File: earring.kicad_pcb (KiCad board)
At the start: 2 copper layers, 41.4 x 41.9 mm, 106 parts, among them J2 USB_C_Receptacle_USB2.0, Q1 Q_NMOS_SGD, Q5 light_sensor, U1 Magnetic Switch, U10 USBLC6-2P6, U20 LGS4056H, U3 RP2040, U4 W25Q16JVUXIQ, U43 TPS22913BYZVR, U44 TPS22913BYZVR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

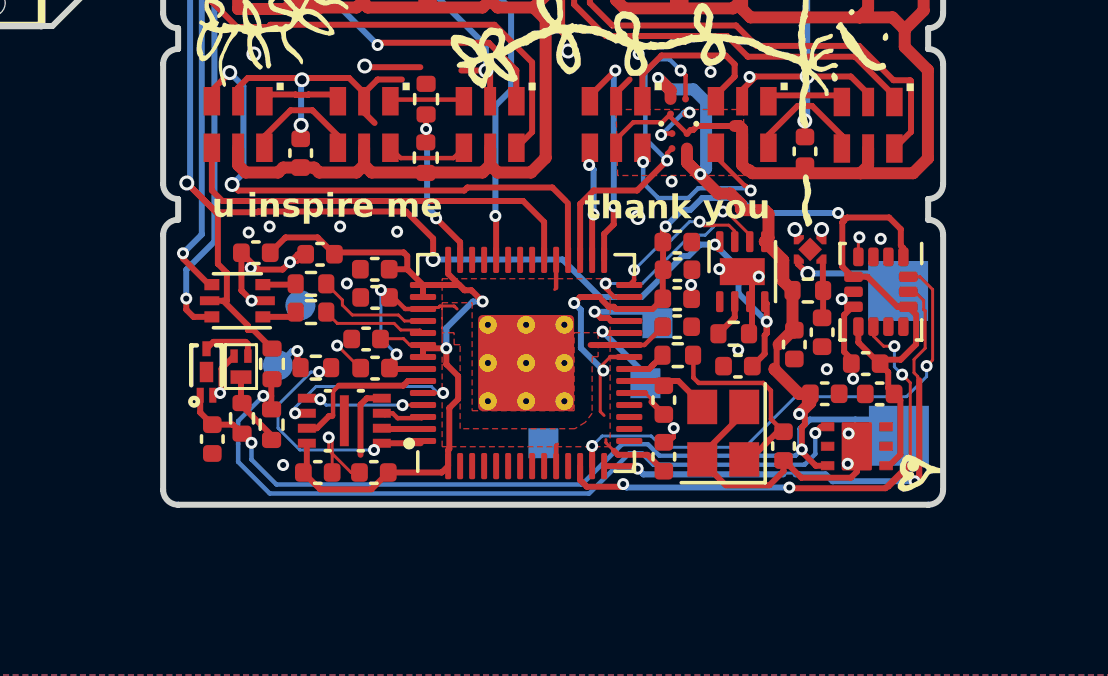
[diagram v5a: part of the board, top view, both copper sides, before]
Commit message: Had to cancel order, fixing DRC issues in progress.
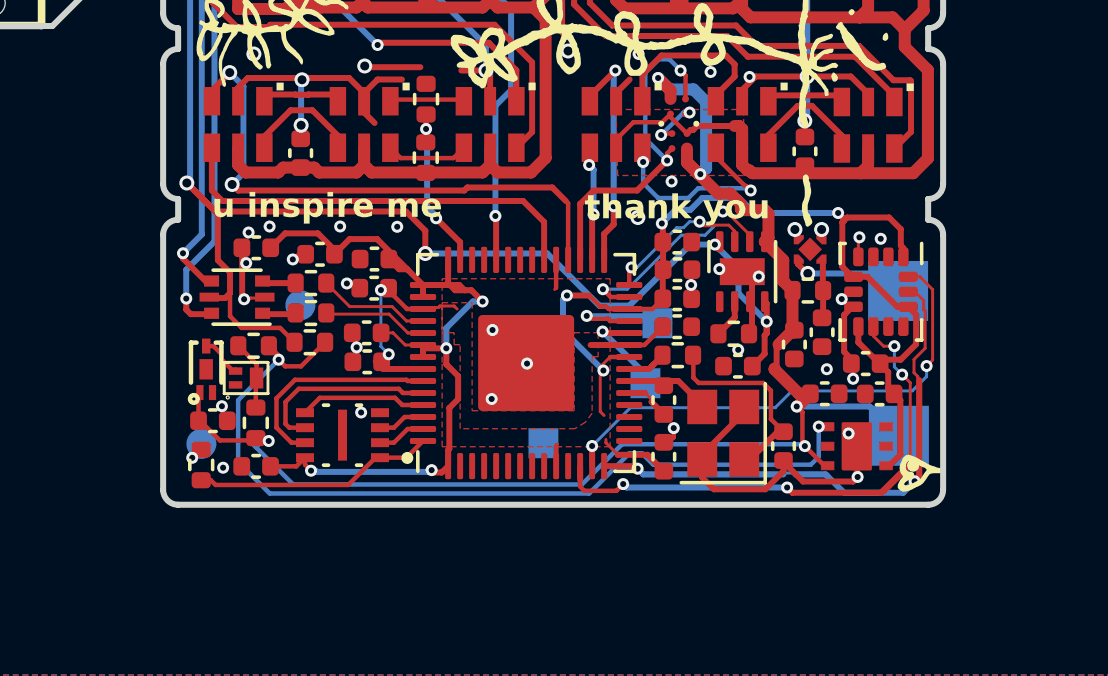
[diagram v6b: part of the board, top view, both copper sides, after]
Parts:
- removed C13: 100n, Capacitor_SMD:C_0402_1005Metric
- C1: value 100n -> 1u
- moved R1 5.01 mm to (151.3, 103.6), turned to 90 degrees
- moved TP7 3.66 mm to (151.3, 102.9)
- moved R15 2.70 mm to (153.0, 99.6), turned to 0 degrees
- moved C1 2.07 mm to (153.1, 103.6), turned to 180 degrees
- moved R2 1.45 mm to (154.9, 99.5), turned to 0 degrees
- moved C19 0.61 mm to (151.7, 102.1), turned to 0 degrees
- moved R13 0.48 mm to (153.1, 102.2)
- moved U4 0.48 mm to (156.0, 102.6)
- moved Q1 0.42 mm to (152.8, 100.7), turned to 0 degrees
- moved C18 0.34 mm to (157.0, 96.7)
- moved C8 0.33 mm to (156.8, 100.2)
- moved C10 0.31 mm to (157.0, 97.7)
- moved C11 0.21 mm to (156.8, 99.2)
- moved C12 0.17 mm to (153.1, 96.4)
- moved U10 0.12 mm to (152.5, 98.0)
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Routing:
- net GND: track 242.7 -> 230.6 mm, vias 95 -> 98
- net /3v3EN: track 25.6 -> 28.5 mm
- net /QSPI_SD3: track 5.00 -> 7.29 mm
- net +3V3: track 64.4 -> 66.4 mm, vias 6 -> 8
- net VBUS: track 55.9 -> 57.4 mm
- net /~{USB_BOOT}: track 1.87 -> 1.01 mm
- net INT: track 21.6 -> 22.2 mm
- net +1V1: track 9.60 -> 10.1 mm
- net /QSPI_SD0: track 3.97 -> 4.24 mm, vias 2 -> 0
- net /QSPI_SS: track 7.86 -> 8.06 mm, vias 2 -> 0
- net /QSPI_SCLK: track 6.18 -> 6.25 mm, vias 2 -> 0

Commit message: more clean up. looking pretty good
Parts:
- moved R12 6.82 mm to (154.6, 86.0)
- moved U43 0.27 mm to (167.3, 93.1)
- moved U8 0.20 mm to (171.6, 96.2)
- moved R4 0.16 mm to (154.0, 84.5)
- moved C17 0.11 mm to (155.1, 96.5)
- moved C4 0.11 mm to (169.2, 100.2)
- moved R8 0.10 mm to (171.4, 71.2)
- moved R3 0.10 mm to (152.0, 84.6)
- moved C28 0.06 mm to (171.5, 93.1)
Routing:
- net /BATT_SENSE: track 5.87 -> 15.1 mm, vias 2 -> 3
- net GND: track 230.6 -> 227.6 mm, vias 98 -> 96
- net +BATT: track 51.0 -> 48.8 mm
- net /LED_1_V: track 224.7 -> 226.5 mm
- net /SW_LED_1: track 11.6 -> 12.6 mm
- net VBUS: track 57.4 -> 58.4 mm
- net Net-(U13-SDO): track 2.95 -> 3.79 mm
- net Net-(U46-CKO): track 2.74 -> 3.45 mm
- net Net-(U13-SDI): track 13.9 -> 14.6 mm
- net +3V3: track 66.4 -> 67.0 mm
- net Net-(U16-CKL): track 15.4 -> 16.0 mm

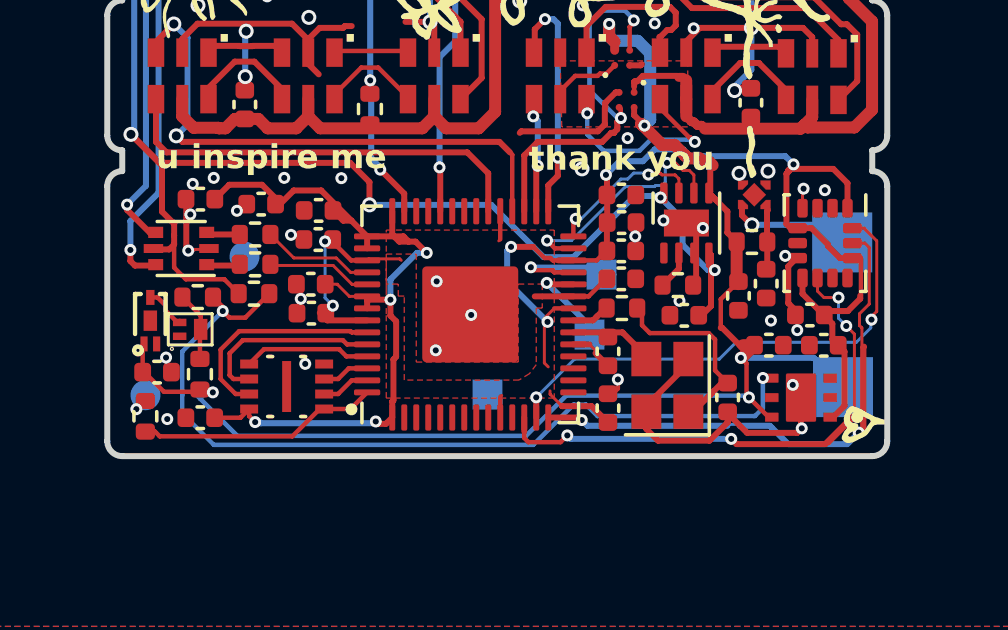
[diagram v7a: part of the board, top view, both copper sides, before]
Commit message: updated with better clearance, ordered this rev after canceling the last order
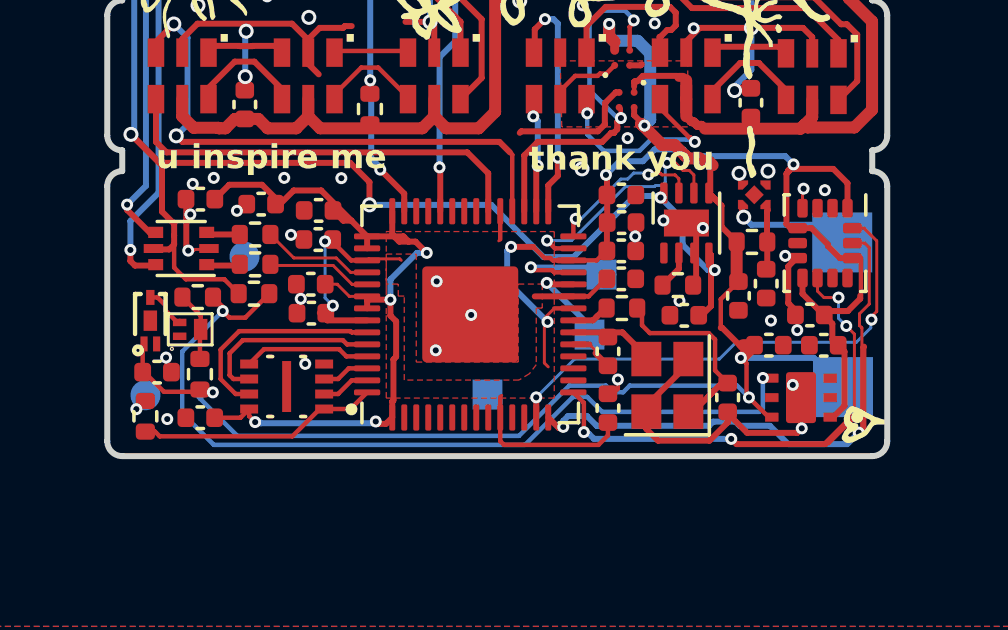
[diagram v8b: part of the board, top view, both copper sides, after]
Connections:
- U3 pad 12: INT -> unconnected-(U3-GPIO9-Pad12)
- U3 pad 15: unconnected-(U3-GPIO12-Pad15) -> INT
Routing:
- net SCL: track 26.9 -> 21.4 mm
- net +3V3: track 67.0 -> 69.5 mm
- net INT: track 22.3 -> 21.0 mm
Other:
- board text added: "I love u"
